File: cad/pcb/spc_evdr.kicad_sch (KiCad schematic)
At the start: 93 parts, among them J1 BL_CONN, SW1 SW_Push, SW10 SW_Push, SW11 SW_Push, SW12 SW_Push, SW13 ON_OFF, SW14 SW_Push, SW15 SW_Push, SW16 SW_Push, SW17 SW_Push, SW18 SW_Push, SW19 SW_Push, SW2 SW_Push, SW20 SW_Push, SW21 SW_Push, SW22 SW_Push, SW23 SW_Push, SW24 SW_Push, SW25 SW_Push, SW26 SW_Push, SW27 SW_Push, SW28 SW_Push, SW29 SW_Push, SW3 SW_Push, SW30 SW_Push, SW31 SW_Push, SW32 SW_Push, SW33 SW_Push, SW34 SW_Push, SW35 SW_Push, SW36 SW_Push, SW37 SW_Push, SW38 SW_Push, SW39 SW_Push, SW4 SW_Push, SW40 SW_Push, SW41 SW_Push, SW42 SW_Push, SW43 SW_Push, SW44 SW_Push, SW45 SW_Push, SW5 RotaryEncoder_Switch, SW6 SW_Push, SW7 SW_Push, SW8 SW_Push, SW9 SW_Push, U1 PCA9555PW, U2 xiao-ble

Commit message: added a whole lot of peripherals
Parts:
- added BZ1: Buzzer, KLOR:Buzzer_Mallory_AST1109MLTRQ_reversible, symbol Device:Buzzer
- added D1, D11, D13, D23, D25, D35, D37, D46: D, weteor:D_SOD-123, symbol Device:D_Small
- added D48, D49, D50, D51, D52: ~, weteor:D_SOD-123, symbol Device:D_Small
- added L1, L2, L3: SK6812MINI, LED_SMD:LED_SK6812MINI_PLCC4_3.5x3.5mm_P1.75mm, symbol kbd:SK6812MINI
- added SW1, SW12, SW15, SW25, SW27, SW37, SW39, SW47: SW_Push, weteor:CherryMX_Hotswap, symbol Switch:SW_Push
- added SW54: SKRHAAE010, mouser:SKRHAAE010, symbol SKRHAAE010:SKRHAAE010
- added U3: Pimoroni haptic buzz, KLOR:Pimoroni Haptic Buzz DRV2605L Driver, symbol Connector_Generic:Conn_01x05
- D39: footprint Diode_SMD:D_SOD-123 -> weteor:D_SOD-123
- SW5: footprint Rotary_Encoder:RotaryEncoder_Alps_EC11E-Switch_Vertical_H20mm -> KLOR:RotaryEncoder_Alps_EC11E-Switch_Vertical_H20mm-keebio_modified
- renumbered D31 to D10, D35 to D12, D2 to D14, D7 to D15, D10 to D16, D13 to D17, D17 to D18, D21 to D19, D1 to D2, D25 to D20, D29 to D21, D32 to D22, D36 to D24, D3 to D26, D8 to D27, D11 to D28, D14 to D29, D6 to D3, D18 to D30, D22 to D31, D26 to D32, D30 to D33, D33 to D34, D37 to D36, D4 to D38, D9 to D4, D5 to D40, D15 to D41, D19 to D42, D23 to D43, D27 to D44, D34 to D45, D38 to D47, D12 to D5, D16 to D6, D20 to D7, D24 to D8, D28 to D9, SW35 to SW10, SW38 to SW11, SW42 to SW14, SW2 to SW16, SW7 to SW17, SW11 to SW18, SW15 to SW19, SW1 to SW2, SW21 to SW20, SW26 to SW21, SW32 to SW22, SW36 to SW23, SW39 to SW24, SW43 to SW26, SW3 to SW28, SW8 to SW29, SW6 to SW3, SW12 to SW30, SW16 to SW31, SW22 to SW32, SW27 to SW33, SW33 to SW34, SW37 to SW35, SW40 to SW36, SW44 to SW38, SW10 to SW4, SW4 to SW40, SW9 to SW41, SW17 to SW42, SW23 to SW43, SW28 to SW44, SW34 to SW45, SW41 to SW46, SW45 to SW48, SW18 to SW49, SW24 to SW50, SW29 to SW51, SW19 to SW52, SW30 to SW53, SW14 to SW6, SW20 to SW7, SW25 to SW8, SW31 to SW9
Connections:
- net +3V3: now also U3.1 (Pin_1)
- net Col_10: now also U1.19 (IO1_6), SW12.1, SW25.1, SW37.1, SW47.1; no longer SW14.1, SW26.1, SW38.1, SW48.1, U2.4 (A11/0.29)
- net Col_5: now also U1.13 (IO1_0); no longer U1.8 (IO0_4)
- net Col_9: now also U1.17 (IO1_4); no longer U2.7 (B8_TX/1.11)
- net GND: now also BZ1.2 (+), L1.2 (VSS), L2.2 (VSS), L3.2 (VSS), U3.5 (Pin_5)
- net Row_1: now also D11.1 (K)
- net Row_2: now also D13.1 (K), D23.1 (K)
- net Row_3: now also D25.1 (K), D35.1 (K)
- net Row_4: now also D37.1 (K), D46.1 (K)
- net scl: now also U3.3 (Pin_3)
- net sda: now also U3.2 (Pin_2)
- net +5V: now reaches U2.14 (5V)
- net +5V: now also L1.4 (VDD), L2.4 (VDD), L3.4 (VDD)
- net LED: now reaches U2.3 (A10/0.28)
- net LED: now also L1.3 (DIN)
- net Col_11: now reaches U1.14 (IO1_1)
- net Col_11: now also SW14.1, SW26.1, SW38.1, SW48.1, D48.2 (A), D49.2 (A), D50.2 (A), D51.2 (A), D52.2 (A)
- new net: D46.2 (A), SW47.2
- new net: D1.2 (A), SW1.2
- new net: D49.1 (K), SW54.2 (CENTER_PUSH)
- new net: D23.2 (A), SW25.2
- new net: D37.2 (A), SW39.2
- new net: L2.1 (DOUT), L3.3 (DIN)
- new net: D50.1 (K), SW54.3 (C)
- new net: D11.2 (A), SW12.2
- new net: D48.1 (K), SW54.1 (A)
- new net: L1.1 (DOUT), L2.3 (DIN)
- new net: D35.2 (A), SW37.2
- new net: D52.1 (K), SW54.6 (D)
- new net: D13.2 (A), SW15.2
- new net: D25.2 (A), SW27.2
- new net: D51.1 (K), SW54.4 (B)
- new net AUDIO: BZ1.1 (-), U2.7 (B8_TX/1.11)
- new net Col_0: SW1.1, SW15.1, SW27.1, SW39.1, U1.8 (IO0_4)
- new net Row_0: SW54.5 (COMMON), U2.4 (A11/0.29)
- no-connect marks 13 -> 9
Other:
- moved on the sheet: BT1, C1, D12, D24, D36, D39, D47, J1, OL1, R1, R2, R3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

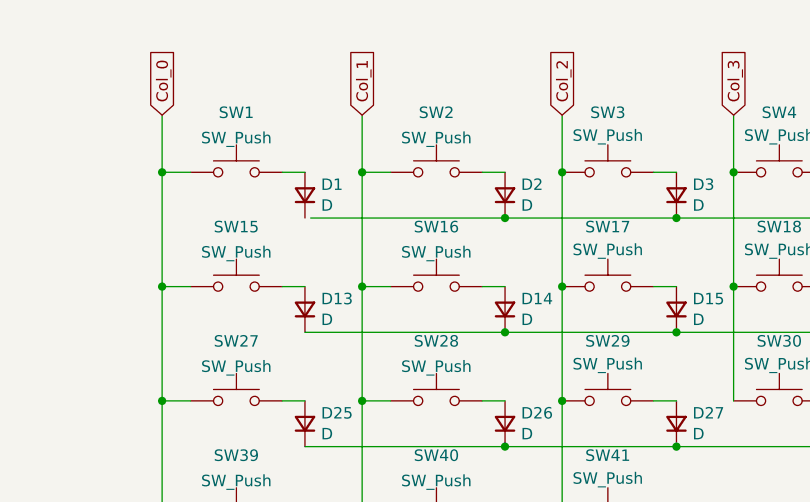
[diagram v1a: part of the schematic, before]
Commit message: fix wire disconnect in matrix
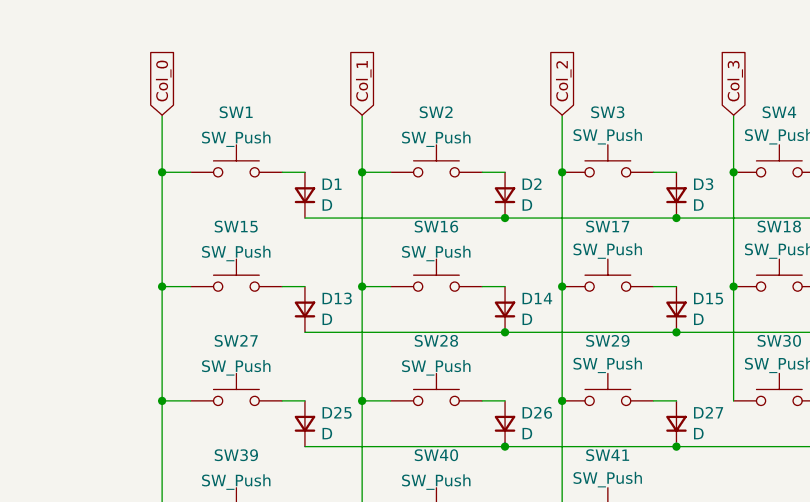
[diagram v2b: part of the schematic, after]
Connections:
- net Row_1: now also D1.1 (K)
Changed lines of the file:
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@@
     (stroke (width 0) (type default))
   )
-  (wire (pts (xy 48.26 30.48) (xy 69.85 30.48))
+  (wire (pts (xy 47.625 30.48) (xy 69.85 30.48))
     (stroke (width 0) (type default))
   )

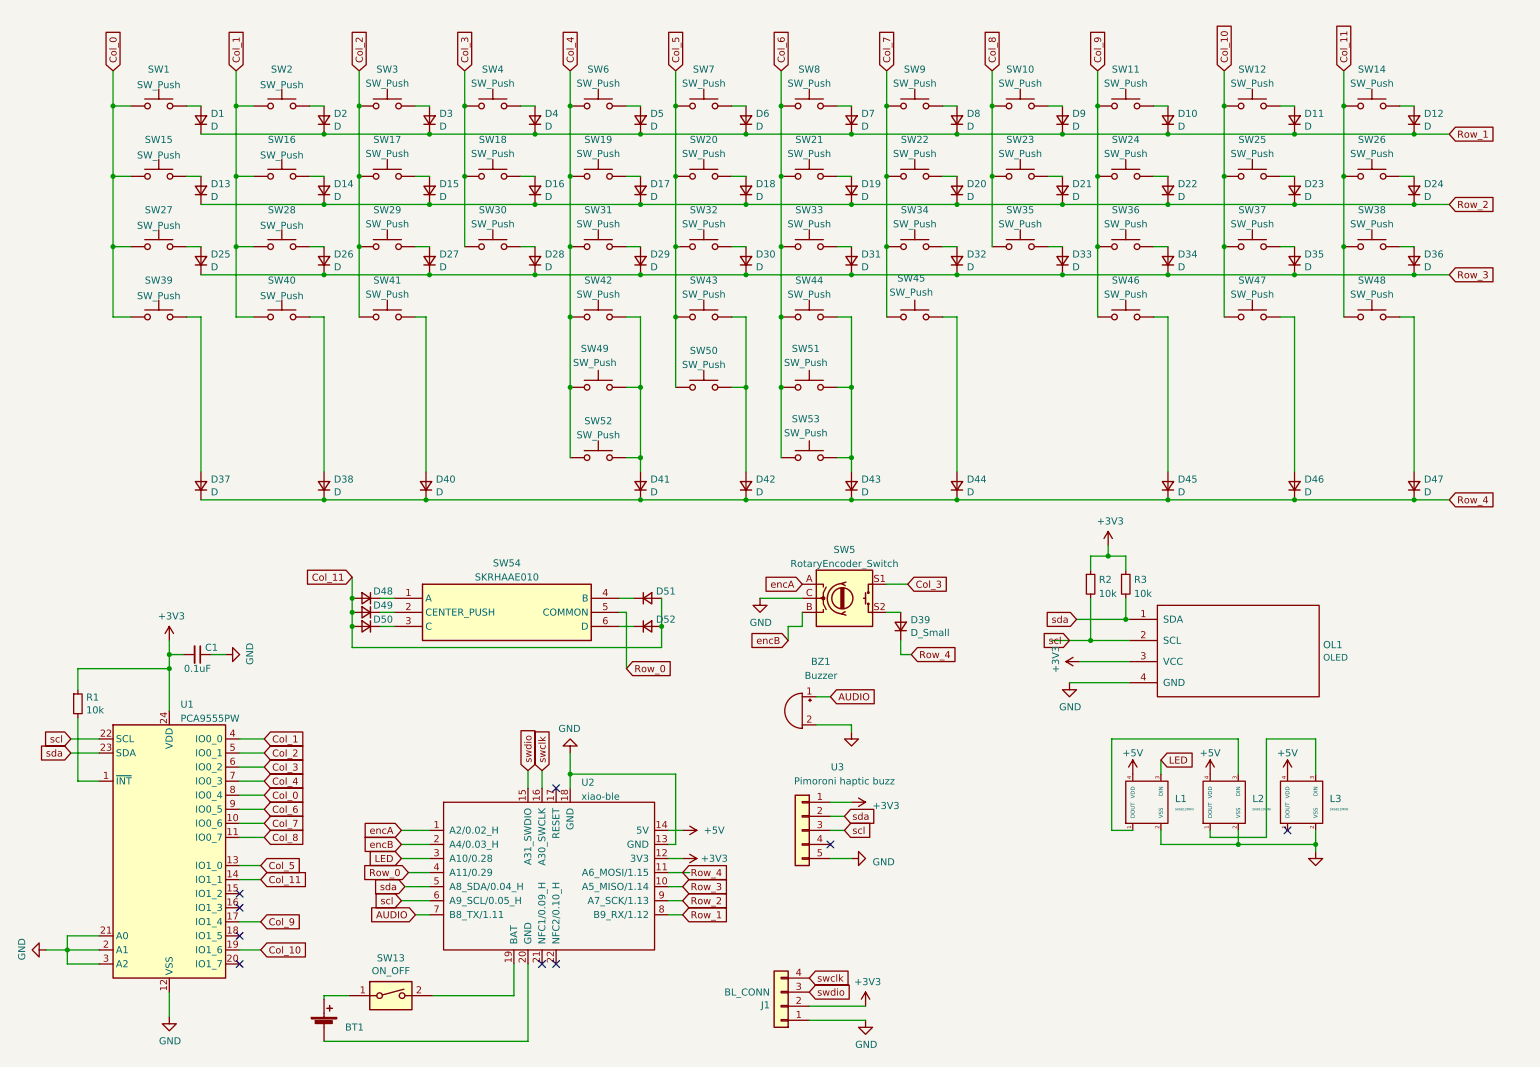
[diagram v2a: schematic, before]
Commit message: 12 col kicad files
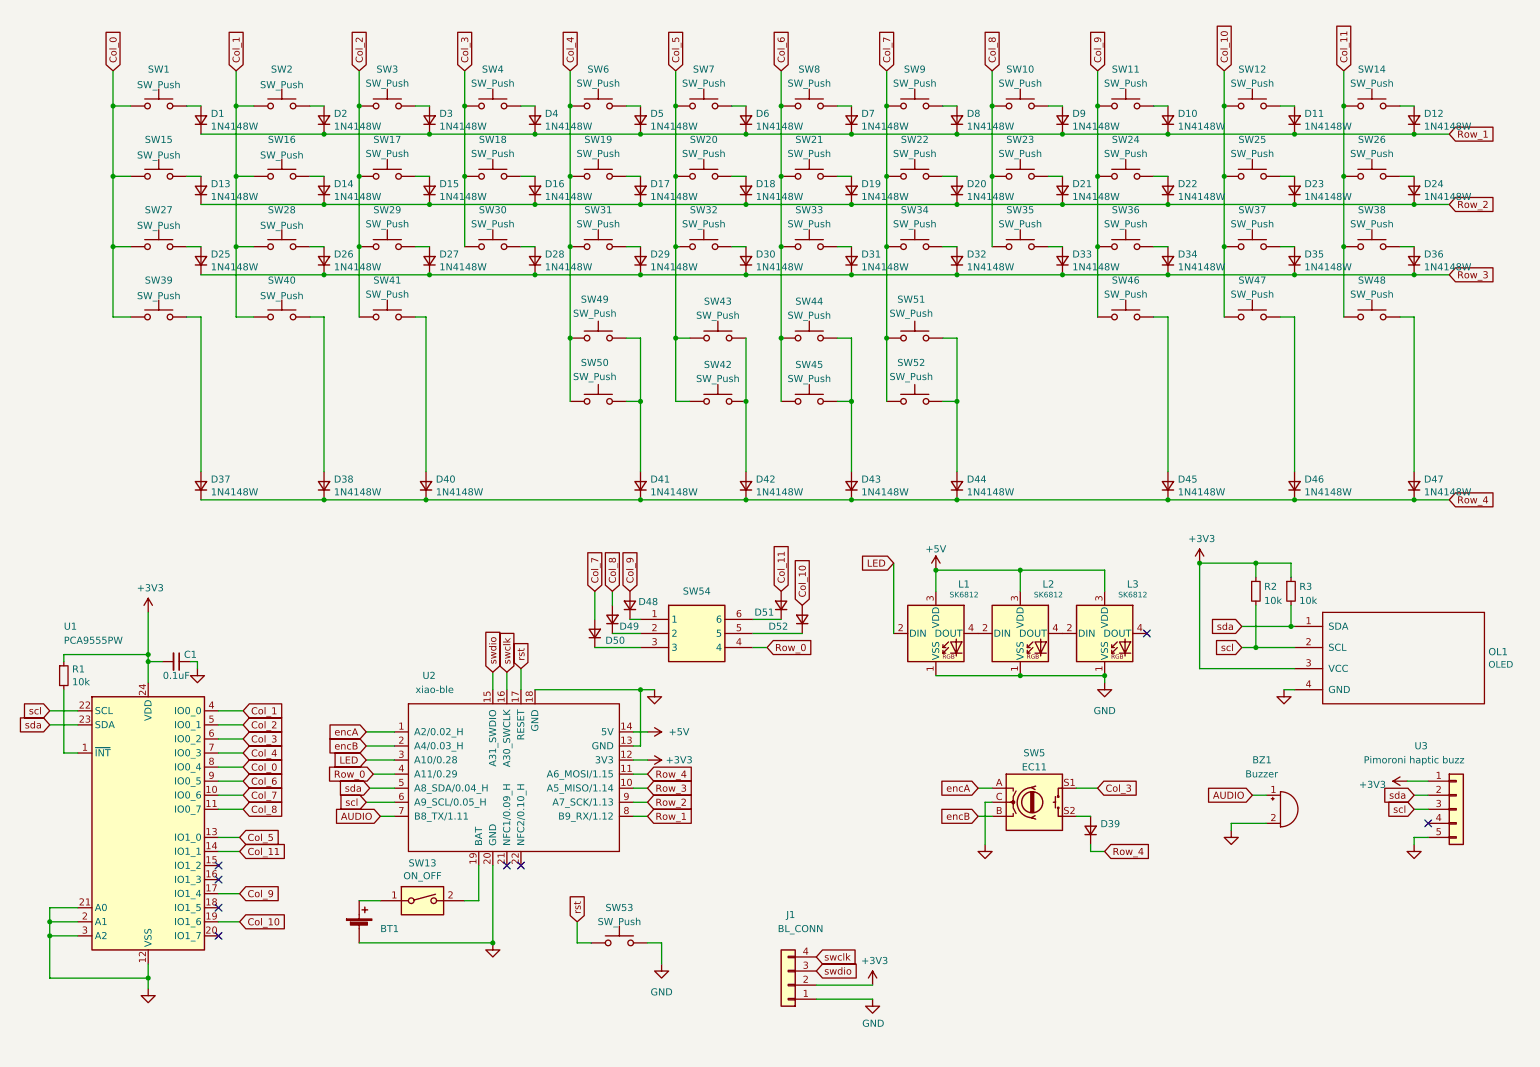
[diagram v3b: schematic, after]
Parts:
- removed L2, L3: SK6812MINI, LED_SMD:LED_SK6812MINI_PLCC4_3.5x3.5mm_P1.75mm, symbol kbd:SK6812MINI
- removed SW51: SW_Push, weteor:CherryMX_Hotswap_1.25u, symbol Switch:SW_Push
- added L2, L3: SK6812, LED_SMD:LED_SK6812_PLCC4_5.0x5.0mm_P3.2mm, symbol LED:SK6812
- added SW45: SW_Push, weteor:Inv_CherryMX_Hotswap_1.25u, symbol Switch:SW_Push
- D1, D10, D11, D12, D13, D14, D15, D16, D17, D18, D19, D2, D20, D21, D22, D23, D24, D25, D26, D27, D28, D29, D3, D30, D31, D32, D33, D34, D35, D36, D37, D38, D4, D40, D41, D42, D43, D44, D45, D46, D47, D5, D6, D7, D8, D9: value D -> 1N4148W
- D39: value D_Small -> 1N4148W
- D48, D49, D50, D51, D52: value ~ -> 1N4148W
- L1: value SK6812MINI -> SK6812; footprint LED_SMD:LED_SK6812MINI_PLCC4_3.5x3.5mm_P1.75mm -> LED_SMD:LED_SK6812_PLCC4_5.0x5.0mm_P3.2mm; symbol kbd:SK6812MINI -> LED:SK6812
- SW42: footprint weteor:CherryMX_Hotswap -> weteor:Inv_CherryMX_Hotswap_1.25u
- SW43, SW44: footprint weteor:CherryMX_Hotswap_1.75u -> weteor:Inv_CherryMX_Hotswap_1.5u
- SW48: footprint weteor:CherryMX_Hotswap -> kbd:CherryMX_1u
- SW49: footprint weteor:CherryMX_Hotswap_1.25u -> weteor:Inv_CherryMX_Hotswap_1.25u
- SW5: value RotaryEncoder_Switch -> EC11
- SW50: footprint weteor:CherryMX_Hotswap_3u_stabs -> weteor:Inv_CherryMX_Hotswap_1.5u
- SW51: renamed from SW45; footprint weteor:CherryMX_Hotswap -> weteor:Inv_CherryMX_Hotswap_1.25u
- SW52: footprint weteor:CherryMX_Hotswap_2.25u_stabs -> weteor:Inv_CherryMX_Hotswap_1.5u
- SW53: footprint weteor:CherryMX_Hotswap_2.25u_stabs -> weteor:Micro_Push_Button_3x6x2.5mm
- SW54: value SKRHAAE010 -> SKQUCAA010; footprint mouser:SKRHAAE010 -> mouser:SKQUCAA010; symbol SKRHAAE010:SKRHAAE010 -> SKQUCAA010:SKQUCAA010; Height (none) -> 10; Manufacturer_Part_Number SKRHAAE010 -> SKQUCAA010; Mouser Part Number 688-SKRHAAE010 -> 688-SKQUCA; Mouser Price/Stock https://www.mouser.co.uk/ProductDetail/Alps-Alpine/SKRHAAE0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 -> https://www.mouser.co.uk/ProductDetail/Alps-Alpine/SKQUCAA0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
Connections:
- net +5V: now also L1.3 (VDD), L2.3 (VDD), L3.3 (VDD); no longer L1.4 (VDD)
- net Col_10: now also D52.2 (A)
- net Col_11: no longer D48.2 (A), D49.2 (A), D50.2 (A), D52.2 (A)
- net Col_4: now also SW50.1; no longer SW42.1, SW52.1
- net Col_5: now also SW42.1; no longer SW50.1
- net Col_6: now also SW45.1; no longer SW53.1
- net Col_7: now also D50.2 (A), SW52.1
- net Col_8: now also D49.2 (A)
- net Col_9: now also D48.2 (A)
- net GND: now also BT1.2 (-), L1.1 (VSS), SW53.2, U2.20 (GND), L2.1 (VSS), L3.1 (VSS); no longer L1.2 (VSS)
- net LED: now also L1.2 (DIN); no longer L1.3 (DIN)
- net Row_0: now also SW54.4; no longer SW54.5 (COMMON)
- net at D42.2 (A), SW43.2: now also SW42.2; no longer SW50.2
- net at D43.2 (A), SW44.2: now also SW45.2; no longer SW53.2
- net at D41.2 (A), SW49.2: now also SW50.2; no longer SW42.2, SW52.2
- net at D52.1 (K): now also SW54.5; no longer SW54.6 (D)
- net at D51.1 (K): now also SW54.6; no longer SW54.4 (B)
- net rst: now reaches U2.17 (RESET)
- net rst: now also SW53.1
- net at D44.2 (A), SW51.2: now also SW52.2
- new net: L2.4 (DOUT), L3.2 (DIN)
- new net: L1.4 (DOUT), L2.2 (DIN)
- no-connect marks 9 -> 8
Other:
- moved on the sheet: BT1, BZ1, C1, D39, D48, D49, D50, D51, D52, J1, OL1, R1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

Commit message: reorganized and fix silkscreens
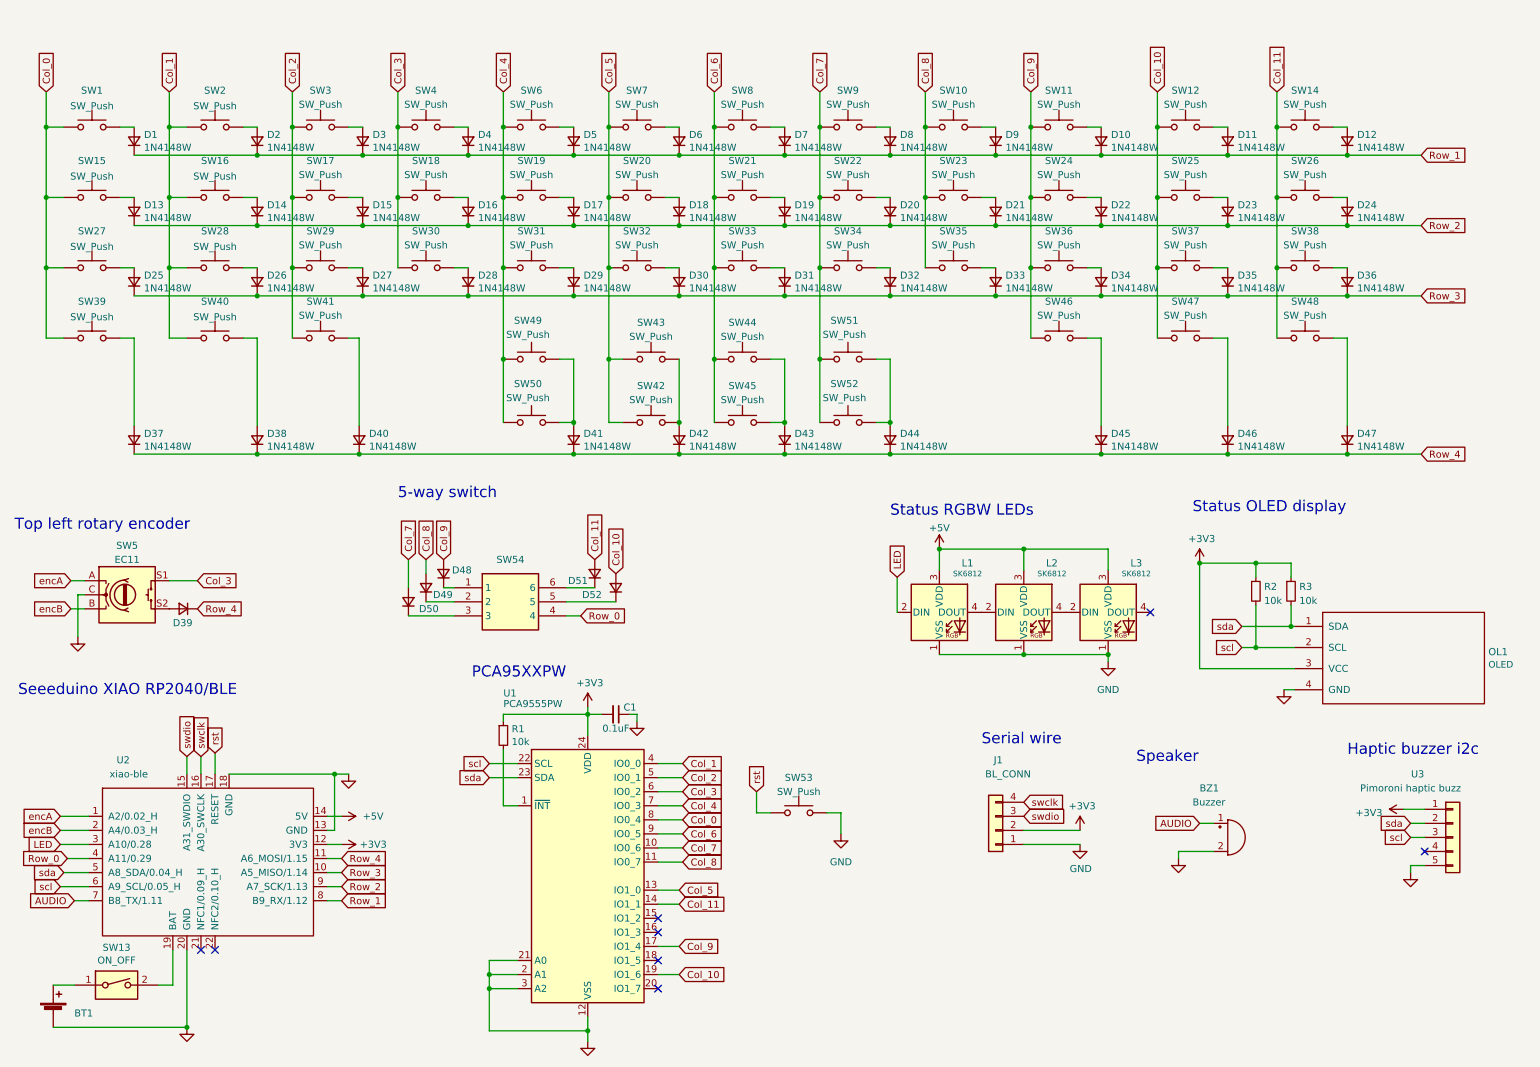
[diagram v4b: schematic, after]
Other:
- note added: "5-way switch"
- note added: "Haptic buzzer i2c"
- note added: "PCA95XXPW"
- note added: "Seeeduino XIAO RP2040/BLE"
- note added: "Serial wire"
- note added: "Speaker"
- note added: "Status OLED display"
- note added: "Status RGBW LEDs"
- note added: "Top left rotary encoder"
- moved on the sheet: BT1, BZ1, C1, D1, D10, D11, D12, D13, D14, D15, D16, D17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
